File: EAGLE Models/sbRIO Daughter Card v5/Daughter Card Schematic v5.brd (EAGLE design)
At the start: 101.6 x 81.3 mm, 81 parts, among them IC1 ITS4880R-PAD, Q1 MMBT4403-7-F, Q10 MMBT4403-7-F, Q11 MMBT4401-7-F, Q13 MMBT4401-7-F, Q2 MMBT4403-7-F, Q7 MMBT4403-7-F, Q8 MMBT4403-7-F, Q9 MMBT4401-7-F, U1 MMBT4403-7-F, U2 ADXL345, U3 L3G4200D

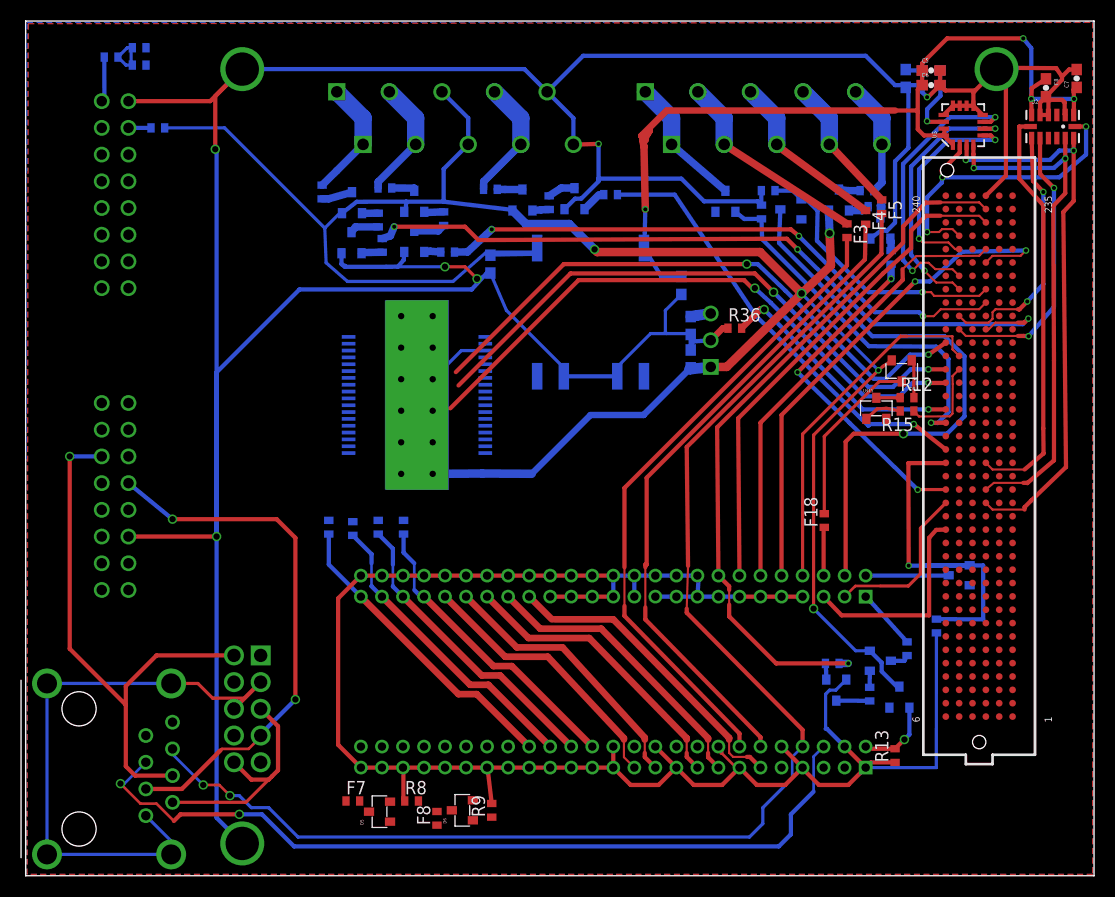
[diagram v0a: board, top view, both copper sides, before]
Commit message: made daughter card amplifiers all based off of  ICs
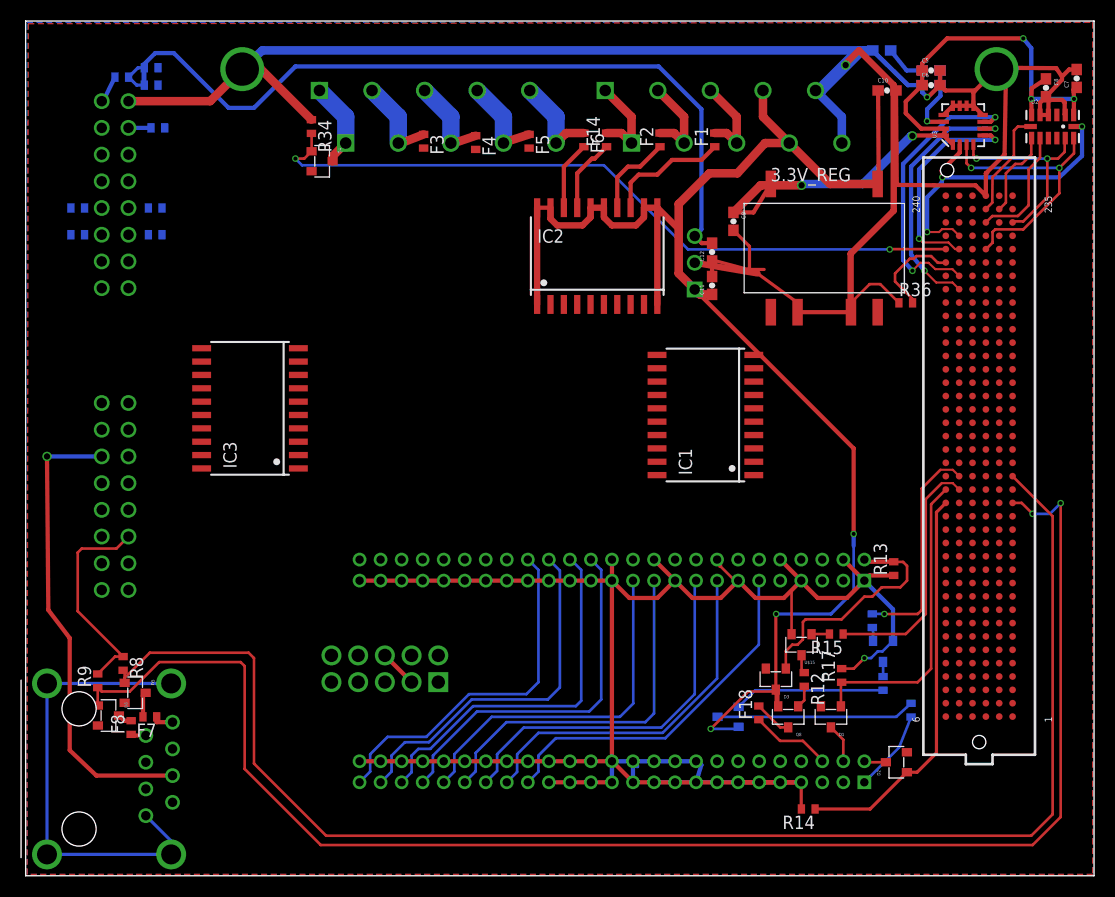
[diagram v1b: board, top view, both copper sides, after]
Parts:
- removed F: (no value), resistor:R0402
- removed Q1, Q10, Q2, U1: MMBT4403-7-F, formula electric:SOT-23-3
- removed Q11, Q13, Q9, U$23: MMBT4401-7-F, formula electric:SOT-23-3
- removed R1, R2, R23, R24, R25, R3: 5k, resistor:R0402
- removed R22, R4: 4.7k, resistor:R0402
- added F14: (no value), resistor:R0402
- added IC2, IC3: BTS716G, infineon:PG-DSO-20
- IC1: value ITS4880R-PAD -> BTS716G; device infineon:PG-DSO-36PAD -> infineon:PG-DSO-20
- moved D1 48.4 mm to (76.6, 15.1), flipped to the top, turned to 180 degrees
- moved R17 46.6 mm to (77.6, 19.1), flipped to the top, turned to 90 degrees
- moved R34 43.6 mm to (27.2, 71.2), flipped to the top
- moved F22 41.6 mm to (4.95, 61.0), turned to 180 degrees
- moved C10 41.2 mm to (81.9, 74.7), flipped to the top, turned to 0 degrees
- moved F3 41.1 mm to (37.8, 69.8)
- moved F20 40.2 mm to (4.95, 63.5), turned to 180 degrees
- moved R9 39.4 mm to (6.86, 18.5)
- moved D4 38.5 mm to (28.2, 67.9), flipped to the top, turned to 270 degrees
- moved F4 37.8 mm to (42.8, 69.7)
- moved F21 35.0 mm to (12.3, 61.0), turned to 0 degrees
- moved D6 34.8 mm to (7.87, 15.2), turned to 270 degrees
- moved Q8 34.6 mm to (72.5, 15.1)
- moved F15 34.6 mm to (12.3, 63.5), turned to 0 degrees
- moved F5 34.1 mm to (47.9, 69.8)
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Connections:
- net DI09 renamed DI02
- net VCC renamed N$5
- removed net N$16: D6.P$2, R9.1, U$3.180
- removed net N$21: IC1.TH@11
- removed net N$36: F.2, SHTDWN_CONN.7, SHTDWN_CONN.8
- removed net N$39: F1.2, SHTDWN_CONN.3, SHTDWN_CONN.4
- removed net N$40: F2.2, SHTDWN_CONN.1, SHTDWN_CONN.2
- removed net N$44: F.1, U1.P$1
- removed net N$45: F6.2, Q10.P$1
- removed net N$46: R23.2, U1.P$2
- removed net N$47: Q1.P$2, R2.2
- removed net N$48: Q2.P$2, R3.2
- removed net N$49: Q10.P$2, R22.2
- removed net N$5 (its old number): IC1.TH@6, IC1.TH@7
- removed net N$7: F1.1, Q1.P$1
- removed net N$73: Q9.P$1, R22.1
- removed net N$74: Q9.P$2, R4.2
- removed net N$75: Q13.P$1, R23.1
- removed net N$76: Q13.P$2, R1.2
- removed net N$77: R2.1, U$23.P$1
- removed net N$78: Q11.P$1, R3.1
- removed net N$79: R24.2, U$23.P$2
- removed net N$8: F2.1, Q2.P$1
- removed net N$80: Q11.P$2, R25.2
- new net BSPD5: F6.2, IC2.18
- new net DIO21: IC2.5, U$3.189
- new net DIO22: IC2.7, U$3.177
- new net DIO4: U$3.192
- new net DIO44: R16.1, U$3.113
- new net DIO45: R15.1, U$3.107
- new net DIO48: U$3.230, U2.8
- new net DIO5: U$3.180
- new net DIO81: U$3.223, U2.12, U3.4
- new net DIO82: U$3.217
- new net DIO83: U$3.205
- new net DIO85: U$3.187
- new net DIO86: U$3.181
- new net DIO87: U$3.169
- new net DIO90: IC3.7, U$3.145
- new net DIO91: IC3.9, U$3.133
- new net DIO92: IC3.3, U$3.127
- new net DIO93: IC3.5, U$3.115
- new net DIO94: D5.P$2, R8.2, U$3.109
- new net DIO95: D6.P$2, R9.1, U$3.97
- new net N$24: U$3.163
- new net SHUTDOWN_1: F14.1, IC2.17
- new net SHUTDOWN_2: F2.1, IC2.14
- new net SHUTDOWN_3: F1.1, IC2.13
- net 12V: now also IC1.1, IC1.10, IC1.11, IC1.12, IC1.15, IC1.16, IC1.19, IC1.20, IC2.1, IC2.10, IC2.11, IC2.12, IC2.15, IC2.16, IC2.19, IC2.20, IC3.1, IC3.10, IC3.11, IC3.12, IC3.15, IC3.16, IC3.19, IC3.20, SHTDWN_CONN.7, SHTDWN_CONN.8; no longer IC1.3, IC1.TH@1, IC1.TH@12, IC1.TH@2, Q1.P$3, Q10.P$3, Q2.P$3, SHTDWN_CONN.5, SHTDWN_CONN.6, U1.P$3
- net AMS_OUT: now also IC3.17; no longer IC1.27, IC1.28
- net BSPD_OUT: now also IC3.13; no longer IC1.23, IC1.24
- net BUZZER_OUT: now also IC3.18; no longer IC1.21, IC1.22
- net DIO1: now also D4.P$2, R34.2
- net DIO10: no longer D4.P$2, R34.2
- net DIO11: no longer R1.1
- net DIO12: no longer D2.P$2, R14.1
- net DIO13: now also D1.P$2, R17.1; no longer R4.1
- net DIO14: now also D2.P$2, R14.1; no longer IC1.13, SBRIO_AUX.P$3
- net DIO15: no longer SBRIO_AUX.P$5
- net DIO16: now also U2.7; no longer R16.1, SBRIO_AUX.P$16
- net DIO17: now also U2.9; no longer SBRIO_AUX.P$14
- net DIO18: now also U2.13, U3.3; no longer SBRIO_AUX.P$12
- net DIO19: no longer SBRIO_AUX.P$10
- net DIO2: now also R36.2
- net DIO20: no longer D1.P$2, R17.1
- net DIO25: now also IC1.3; no longer IC1.6
- net DIO26: now also IC1.5; no longer IC1.7
- net DIO27: now also IC1.7; no longer IC1.8
- net DIO29: no longer U2.7
- net DIO30: no longer U2.12, U3.4
- net DIO31: no longer U2.13, U3.3
- net DIO36: no longer U2.8
- net DIO37: no longer U2.9
- net DIO38: no longer SBRIO_AUX.P$8
- net DIO39: no longer R15.1
- net DIO6: now also IC2.3; no longer IC1.10
- net DIO7: now also IC2.9; no longer IC1.11
- net DIO8: no longer IC1.12
- net DIO9: no longer R36.2
- net GND: now also IC1.2, IC1.6, IC3.2, IC3.6; no longer IC1.19, Q11.P$3, Q13.P$3, Q9.P$3, U$23.P$3
- net IMD_OUT: now also IC3.14; no longer IC1.25, IC1.26
- net N$11: now also F1.2, SHTDWN_CONN.5, SHTDWN_CONN.6; no longer R24.1, U$3.189
- net N$12: now also F2.2, SHTDWN_CONN.3, SHTDWN_CONN.4; no longer R25.1, U$3.177
- net N$15: now also F14.2, SHTDWN_CONN.1, SHTDWN_CONN.2; no longer D5.P$2, R8.2, U$3.192
- net PO1: now also IC1.18; no longer IC1.35, IC1.36
- net PO2: now also IC1.17; no longer IC1.33, IC1.34
- net PO3: now also IC1.14; no longer IC1.31, IC1.32
- net PO4: now also IC1.13; no longer IC1.29, IC1.30
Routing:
- net DIO95: track 0.00 -> 143.9 mm, vias 0 -> 2
- net DIO94: track 0.00 -> 138.6 mm
- net AI2: track 132.3 -> 0.00 mm, vias 2 -> 0
- net GND: track 548.5 -> 449.2 mm, vias 11 -> 5
- net AI1: track 80.1 -> 0.00 mm, vias 2 -> 0
- net 12V: track 235.7 -> 156.2 mm, vias 5 -> 3
- net 5V: track 7.04 -> 80.5 mm
- net DIO1: track 0.00 -> 69.0 mm, vias 0 -> 2
- net AI3: track 62.9 -> 0.00 mm
- net N$12: track 70.6 -> 8.72 mm, vias 3 -> 0
- net AI4: track 61.6 -> 0.00 mm
- net DIO16: track 68.0 -> 10.3 mm, vias 1 -> 0
- net DIO8: track 57.4 -> 0.00 mm, vias 2 -> 0
- net DIO6: track 56.6 -> 0.00 mm, vias 2 -> 0
- net DIO7: track 55.9 -> 0.00 mm, vias 2 -> 0
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
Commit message: more daughter card work
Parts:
- moved Q7 13.9 mm to (80.3, 18.7), flipped to the top
- moved R14 12.8 mm to (83.4, 15.5), turned to 270 degrees
- moved D2 4.89 mm to (80.5, 15.1), turned to 180 degrees
- moved AIO_PO_CONN 3.43 mm to (11.2, 66.9)
- moved F10 3.43 mm to (14.6, 77.3)
- moved F15 3.43 mm to (15.0, 65.7)
- moved F16 3.43 mm to (11.8, 78.1)
- moved F20 3.43 mm to (7.62, 65.7)
- moved F9 3.43 mm to (14.6, 79.0)
- moved F21 3.43 mm to (15.0, 63.1)
- moved F22 3.43 mm to (7.62, 63.1)
- moved TUB_CONN 3.43 mm to (11.2, 38.2)
- moved F19 3.43 mm to (15.2, 73.3)
- moved R11 3.25 mm to (79.9, 21.1), flipped to the top, turned to 180 degrees
- moved R16 3.14 mm to (83.6, 25.0), flipped to the top, turned to 180 degrees
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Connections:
- net AI1: now also ACCUMULATOR_CONN.2; no longer ACCUMULATOR_CONN.5
- net AI2: now also ACCUMULATOR_CONN.3; no longer ACCUMULATOR_CONN.6
- net CAN_H: now also ACCUMULATOR_CONN.5; no longer ACCUMULATOR_CONN.3
- net DIO94: now also D6.P$2, R9.1; no longer D5.P$2, R8.2
- net DIO95: now also D5.P$2, R8.2; no longer D6.P$2, R9.1
- net SHIELD: now also ACCUMULATOR_CONN.6; no longer ACCUMULATOR_CONN.2
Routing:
- net CAN_L: track 44.6 -> 80.6 mm, vias 1 -> 2
- net GND: track 449.2 -> 422.5 mm, vias 5 -> 7
- net SHIELD: track 0.00 -> 26.0 mm, vias 0 -> 1
- net CAN_GND: track 48.1 -> 72.6 mm, vias 0 -> 1
- net CAN_H: track 0.00 -> 22.8 mm, vias 0 -> 1
- net DIO95: track 143.9 -> 125.9 mm, vias 2 -> 0
- net N$56: track 18.9 -> 2.18 mm
- net N$54: track 14.4 -> 1.48 mm
- net DIO14: track 37.9 -> 25.3 mm
- net N$55: track 7.79 -> 12.7 mm
- net DIO94: track 138.6 -> 133.8 mm
- net 12V: track 156.2 -> 152.2 mm, vias 3 -> 2
- net DIO44: track 21.0 -> 17.3 mm, vias 1 -> 0
- net DIO13: track 29.0 -> 27.3 mm
- net N$1: track 2.09 -> 3.51 mm
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
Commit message: made more changes to daughter card
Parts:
- removed F10, F9: (no value), resistor:R0402
- added F11, F12: (no value), resistor:R0402
- moved IC3 2.17 mm to (21.6, 42.3)
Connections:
- removed net N$22: F9.1, TUB_CONN.12
- removed net N$23: F10.1, TUB_CONN.5
- new net N$7: F11.1, TUB_CONN.3
- new net N$8: F12.1, TUB_CONN.1
- net 12V: now also F11.2
- net 5V: now also F12.2; no longer F10.2, F9.2
- net AI3: now also TUB_CONN.11; no longer TUB_CONN.10
- net AI4: now also TUB_CONN.12; no longer TUB_CONN.9
- net AMS_OUT: now also TUB_CONN.6; no longer TUB_CONN.3
- net BSPD_OUT: now also TUB_CONN.4; no longer TUB_CONN.1
- net BUZZER_OUT: now also TUB_CONN.7; no longer TUB_CONN.4
- net CAN_H: now also TUB_CONN.9; no longer TUB_CONN.7
- net CAN_L: now also TUB_CONN.8; no longer TUB_CONN.6
- net DI02: now also TUB_CONN.2; no longer TUB_CONN.8
- net GND: now also TUB_CONN.10; no longer TUB_CONN.11
- net IMD_OUT: now also TUB_CONN.5; no longer TUB_CONN.2
- net STEERING_POS: now also TUB_CONN.16; no longer TUB_CONN.14
- net THROTTLE_1: now also TUB_CONN.15; no longer TUB_CONN.16
- net THROTTLE_2: now also TUB_CONN.14; no longer TUB_CONN.15
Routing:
- net GND: track 422.5 -> 495.7 mm
- net STEERING_POS: track 34.4 -> 82.8 mm
- net CAN_H: track 22.8 -> 60.8 mm
- net CAN_L: track 80.6 -> 76.7 mm, vias 2 -> 1
- net 5V: track 79.8 -> 77.0 mm
- net CAN_GND: track 72.6 -> 73.7 mm

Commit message: more daughter card  revisions
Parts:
- removed F11, F12: (no value), resistor:R0402
- added F10, F9: (no value), resistor:R0402
- moved IC1 43.9 mm to (22.9, 57.3)
- moved R36 2.53 mm to (84.5, 56.9), turned to 90 degrees
- moved IC3 1.02 mm to (22.6, 42.2)
- moved 3.3V_REG 0.92 mm to (75.2, 59.2)
- moved F16 0.81 mm to (12.4, 77.6)
- moved U3 0.63 mm to (88.5, 71.4)
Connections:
- removed net DI02: TUB_CONN.2
- removed net N$7: F11.1, TUB_CONN.3
- removed net N$8: F12.1, TUB_CONN.1
- new net DIO64: U$3.226, U3.6
- new net DIO65: U$3.220, U3.7
- new net N$16: F9.1, TUB_CONN.3
- new net N$17: F10.1, TUB_CONN.1
- net 12V: now also F9.2; no longer F11.2
- net 5V: now also F10.2; no longer F12.2
- net AI7: now also TUB_CONN.15; no longer TUB_CONN.13
- net DIO0: now also U2.14, U3.2
- net DIO2: now also TUB_CONN.2
- net DIO32: now also U3.5; no longer U2.14, U3.2
- net DIO33: no longer U3.5
- net DIO34: no longer U3.7
- net DIO35: no longer U3.6
- net THROTTLE_1: now also TUB_CONN.13; no longer TUB_CONN.15
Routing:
- net AI2: track 0.00 -> 83.3 mm, vias 0 -> 1
- net AI1: track 0.00 -> 83.1 mm, vias 0 -> 1
- net DIO34: track 27.7 -> 0.00 mm, vias 2 -> 0
- net DIO0: track 0.00 -> 27.5 mm, vias 0 -> 2
- net DIO35: track 25.1 -> 0.00 mm, vias 2 -> 0
- net DIO33: track 20.6 -> 0.00 mm, vias 2 -> 0
- net DIO32: track 30.6 -> 12.1 mm, vias 3 -> 0
- net GND: track 495.7 -> 509.5 mm
- net DIO65: track 0.00 -> 13.3 mm
- net DIO64: track 0.00 -> 11.4 mm
- net 5V: track 77.0 -> 69.9 mm
- net DIO2: track 9.27 -> 3.29 mm
- net STEERING_POS: track 82.8 -> 79.4 mm
- net DIO94: track 133.8 -> 131.8 mm
- net DIO95: track 125.9 -> 124.0 mm
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
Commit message: FINISHED DAUGHTER CARD LAYOUT
haven't run DRC  yet
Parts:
- moved R36 78.8 mm to (6.86, 43.3)
- moved F3 53.5 mm to (83.9, 42.8), flipped to the bottom
- moved F4 47.1 mm to (81.4, 42.8), flipped to the bottom
- moved F5 41.1 mm to (78.9, 42.8), flipped to the bottom
- moved C10 8.76 mm to (73.5, 72.1)
- moved F22 8.50 mm to (15.9, 61.1), turned to 0 degrees
- moved F20 8.39 mm to (15.9, 64.1), turned to 0 degrees
- moved F19 7.38 mm to (7.87, 73.7), flipped to the top, turned to 90 degrees
- moved F16 5.74 mm to (6.99, 75.8), flipped to the top
- moved IC1 4.01 mm to (22.1, 53.3)
- moved F9 3.30 mm to (14.7, 44.6), turned to 0 degrees
- moved R35 2.62 mm to (82.4, 76.1), flipped to the top, turned to 90 degrees
- moved IC3 2.09 mm to (22.1, 40.1)
- moved C9 1.97 mm to (65.4, 62.7)
- moved F21 1.02 mm to (15.9, 62.6)
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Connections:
- new net DIO40: IC1.7, U$3.149
- new net DIO41: IC1.5, U$3.143
- new net DIO42: IC3.7, U$3.131
- new net DIO43: IC3.5, U$3.125
- net AI10: now also AIO_PO_CONN.7; no longer AIO_PO_CONN.5
- net AI8: now also AIO_PO_CONN.5; no longer AIO_PO_CONN.7
- net AO0: now also F15.1; no longer F22.1
- net AO1: now also F20.1; no longer F21.1
- net AO2: now also F21.1; no longer F20.1
- net AO3: now also F22.1; no longer F15.1
- net DIO10: now also IC3.9
- net DIO11: now also IC3.3
- net DIO12: now also R36.2, TUB_CONN.2
- net DIO2: no longer R36.2, TUB_CONN.2
- net DIO21: no longer IC2.5
- net DIO22: no longer IC2.7
- net DIO25: no longer IC1.3
- net DIO26: no longer IC1.5
- net DIO27: no longer IC1.7
- net DIO28: no longer IC1.9
- net DIO38: now also IC2.7
- net DIO39: now also IC2.5
- net DIO6: now also IC2.9; no longer IC2.3
- net DIO7: now also IC2.3; no longer IC2.9
- net DIO8: now also IC1.9
- net DIO9: now also IC1.3
- net DIO90: no longer IC3.7
- net DIO91: no longer IC3.9
- net DIO92: no longer IC3.3
- net DIO93: no longer IC3.5
- net GND: now also IC2.2, IC2.6
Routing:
- net 12V: track 151.4 -> 282.6 mm, vias 2 -> 7
- net AI4: track 0.00 -> 116.5 mm, vias 0 -> 3
- net GND: track 509.5 -> 624.0 mm, vias 7 -> 10
- net DIO12: track 0.00 -> 106.1 mm, vias 0 -> 1
- net AI11: track 34.4 -> 130.0 mm, vias 0 -> 2
- net AI9: track 0.00 -> 95.4 mm
- net AI8: track 0.00 -> 94.0 mm
- net AI10: track 0.00 -> 88.9 mm
- net AI3: track 0.00 -> 85.8 mm, vias 0 -> 1
- net N$53: track 8.64 -> 91.6 mm
- net AI15: track 33.8 -> 111.4 mm
- net N$52: track 8.56 -> 84.1 mm
- net N$43: track 8.62 -> 77.8 mm
- net DIO42: track 0.00 -> 67.1 mm
- net DIO10: track 0.00 -> 66.5 mm
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
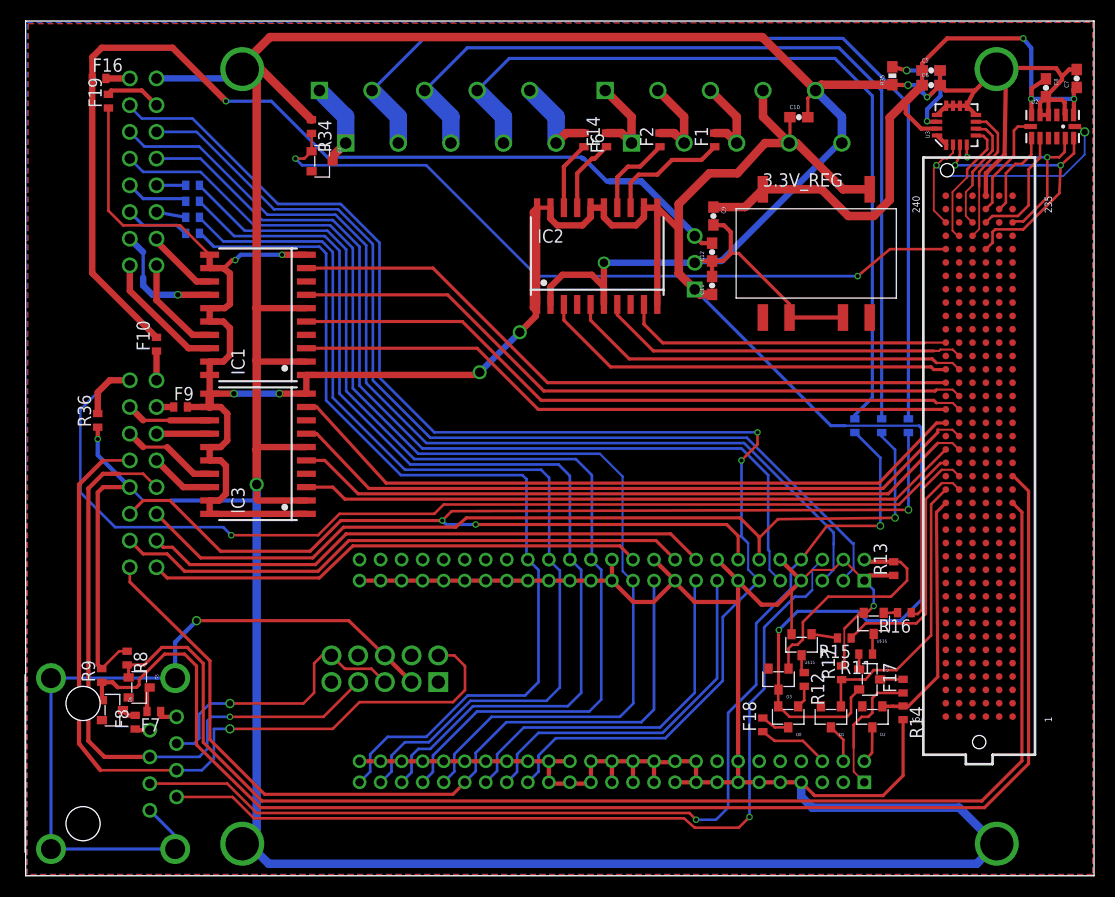
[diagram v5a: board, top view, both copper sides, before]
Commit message: Routed extra DIO, because it was easy
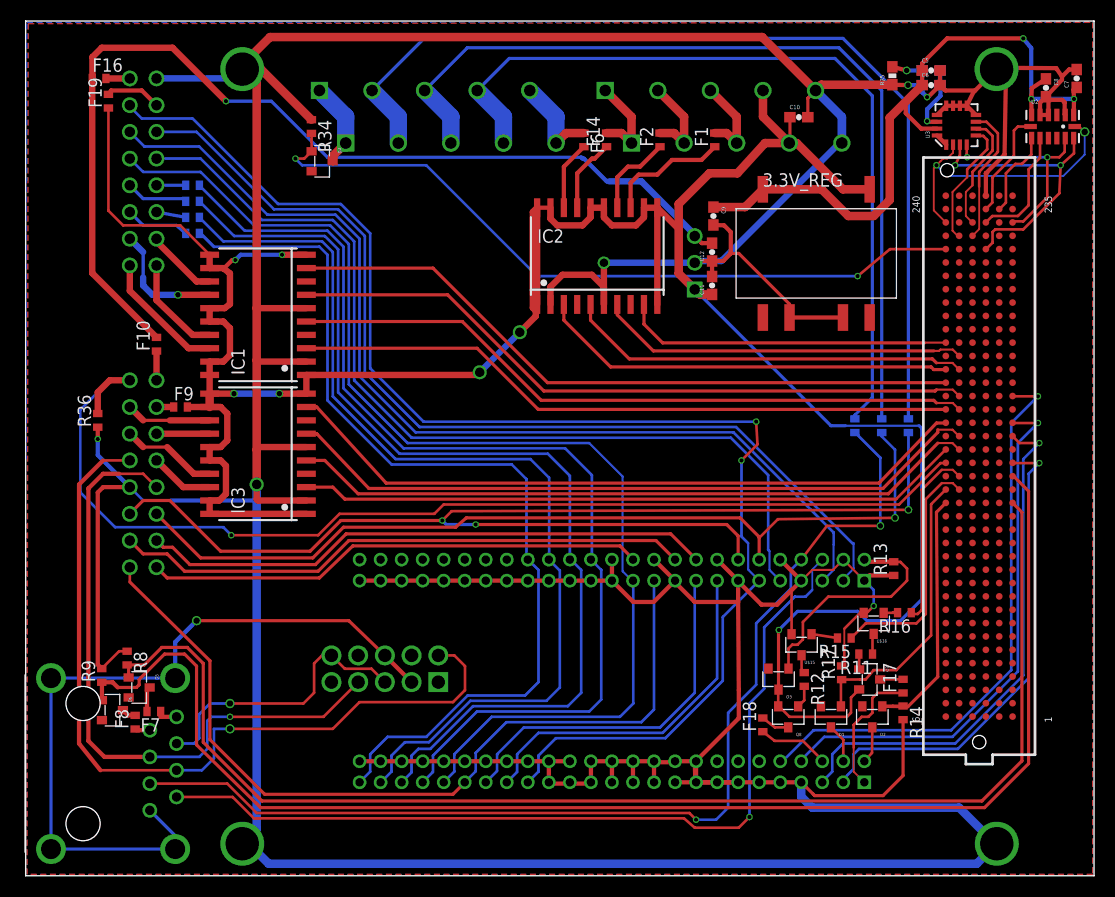
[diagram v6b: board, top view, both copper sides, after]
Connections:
- new net DIO89: SBRIO_AUX.P$12
- net DIO90: now also SBRIO_AUX.P$10
- net DIO91: now also SBRIO_AUX.P$8
- net DIO92: now also SBRIO_AUX.P$5
- net DIO93: now also SBRIO_AUX.P$3
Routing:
- net DIO90: track 0.00 -> 55.1 mm, vias 0 -> 1
- net DIO91: track 0.00 -> 51.1 mm, vias 0 -> 1
- net DIO92: track 0.00 -> 49.9 mm, vias 0 -> 1
- net DIO93: track 0.00 -> 46.1 mm, vias 0 -> 1
- net GND: track 624.0 -> 629.7 mm
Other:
- board text added: "Design By: Thomas Wilson & Michael DeLay"
- board text added: "Layout By: Michael DeLay"
- board text removed: "Design By: Thomas Willson"
- board text removed: "Layout By: Kendall Searing"
